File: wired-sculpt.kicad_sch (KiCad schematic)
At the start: 40 parts, among them J1 USB_C_Receptacle, J2 FFC3B07-30-T, J3 AVR-ISP-6 - NOT FITTED, Q1 BSS84AK,215, Q2 2N7002BK,215, SW1 FSMSM, U1 USBLC6-2SC6, U2 LM2776DBVT, U3 AT90USB1286-AUR, Y1 TSX-3225 16.0000MF18X-AC0

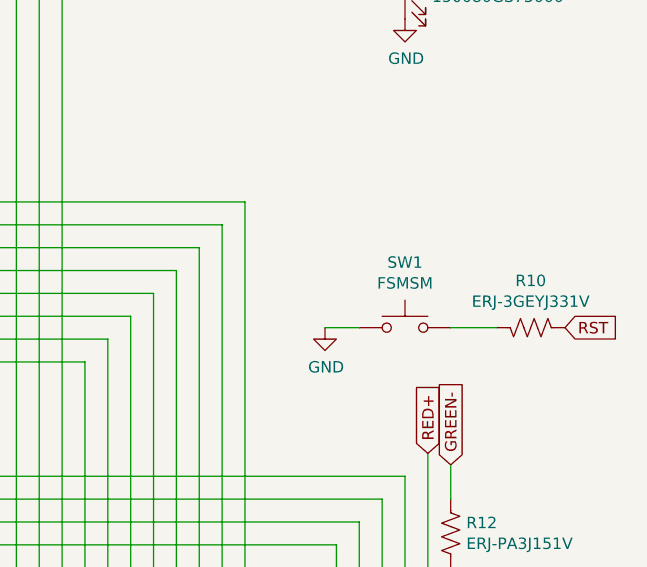
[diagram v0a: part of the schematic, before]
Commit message: Change reset switch to horizontal
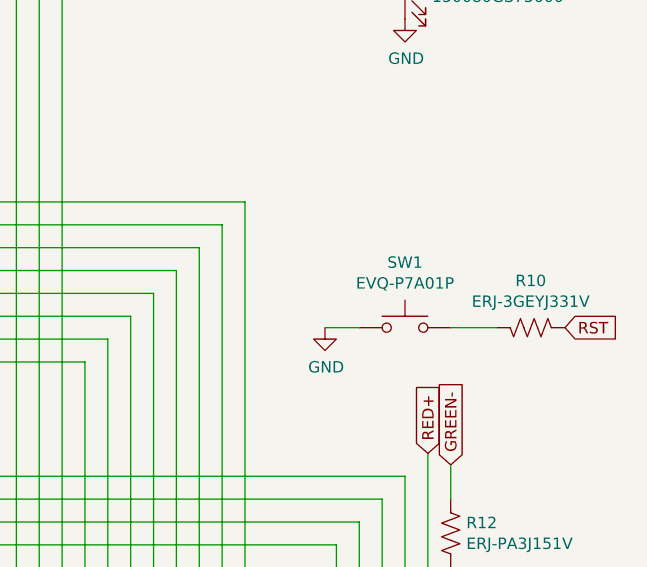
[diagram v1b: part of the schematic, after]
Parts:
- SW1: value FSMSM -> EVQ-P7A01P; footprint Button_Switch_SMD:SW_SPST_FSMSM -> Button_Switch_SMD:SW_SPST_EVQP7A; MPN FSMSM -> EVQ-P7A01P
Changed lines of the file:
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@@
     (in_bom yes) (on_board yes)
     (property "Reference" "SW1" (id 0) (at 234.95 95.631 0))
-    (property "Value" "FSMSM" (id 1) (at 234.95 97.9424 0))
-    (property "Footprint" "Button_Switch_SMD:SW_SPST_FSMSM" (id 2) (at 234.95 97.79 0)
+    (property "Value" "EVQ-P7A01P" (id 1) (at 234.95 97.9424 0))
+    (property "Footprint" "Button_Switch_SMD:SW_SPST_EVQP7A" (id 2) (at 234.95 97.79 0)
       (effects (font (size 1.27 1.27)) hide)
     )
@@
       (effects (font (size 1.27 1.27)) hide)
     )
-    (property "MPN" "FSMSM" (id 4) (at 234.95 102.87 0)
+    (property "MPN" "EVQ-P7A01P" (id 4) (at 234.95 102.87 0)
       (effects (font (size 1.27 1.27)) hide)
     )
@@
     )
     (path "/00000000-0000-0000-0000-00005fce3ca5"
-      (reference "SW1") (unit 1) (value "FSMSM") (footprint "Button_Switch_SMD:SW_SPST_FSMSM")
+      (reference "SW1") (unit 1) (value "EVQ-P7A01P") (footprint "Button_Switch_SMD:SW_SPST_EVQP7A")
     )
     (path "/00000000-0000-0000-0000-00005fcb764b"

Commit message: Increase H3 to 3mm
Slightly more tolerance is needed. Board fit in one of my keyboards, but
not the other
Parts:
- H3: footprint MountingHole:MountingHole_2.7mm -> MountingHole:MountingHole_3mm
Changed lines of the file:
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@@
       (effects (font (size 1.27 1.27)) (justify left))
     )
-    (property "Footprint" "MountingHole:MountingHole_2.7mm" (id 2) (at 132.08 193.04 0)
+    (property "Footprint" "MountingHole:MountingHole_3mm" (id 2) (at 132.08 193.04 0)
       (effects (font (size 1.27 1.27)) hide)
     )
@@
     )
     (path "/00000000-0000-0000-0000-00005fc9a3d1"
-      (reference "H3") (unit 1) (value "AlignmentHole") (footprint "MountingHole:MountingHole_2.7mm")
+      (reference "H3") (unit 1) (value "AlignmentHole") (footprint "MountingHole:MountingHole_3mm")
     )
     (path "/00000000-0000-0000-0000-00005fc1fde4"

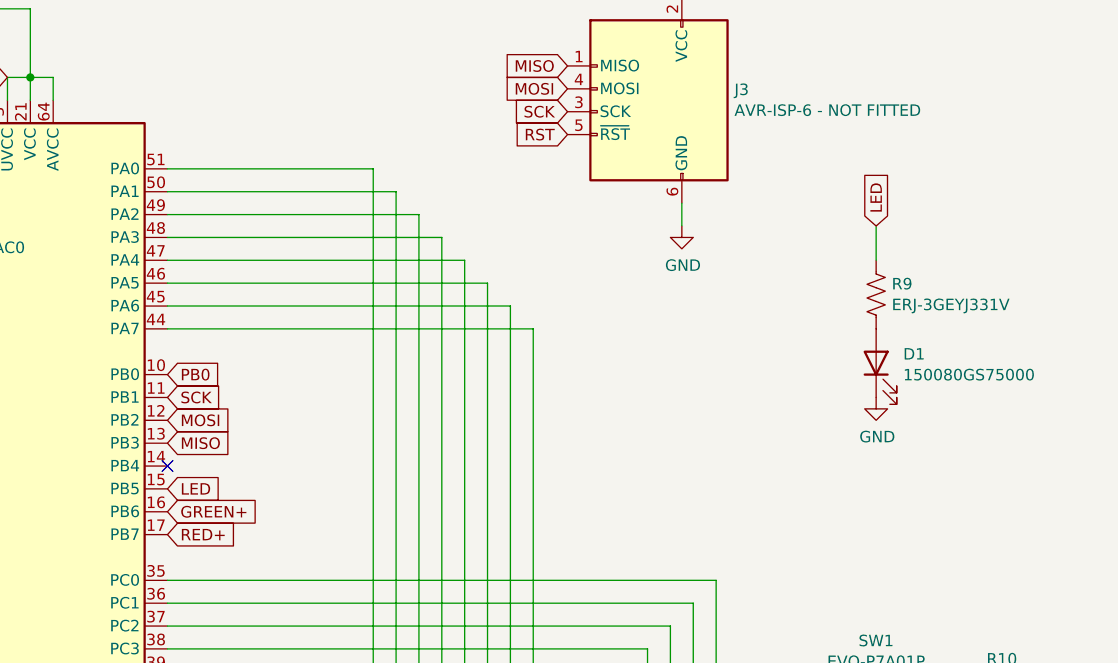
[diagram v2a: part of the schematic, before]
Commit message: Remove on-board status LED
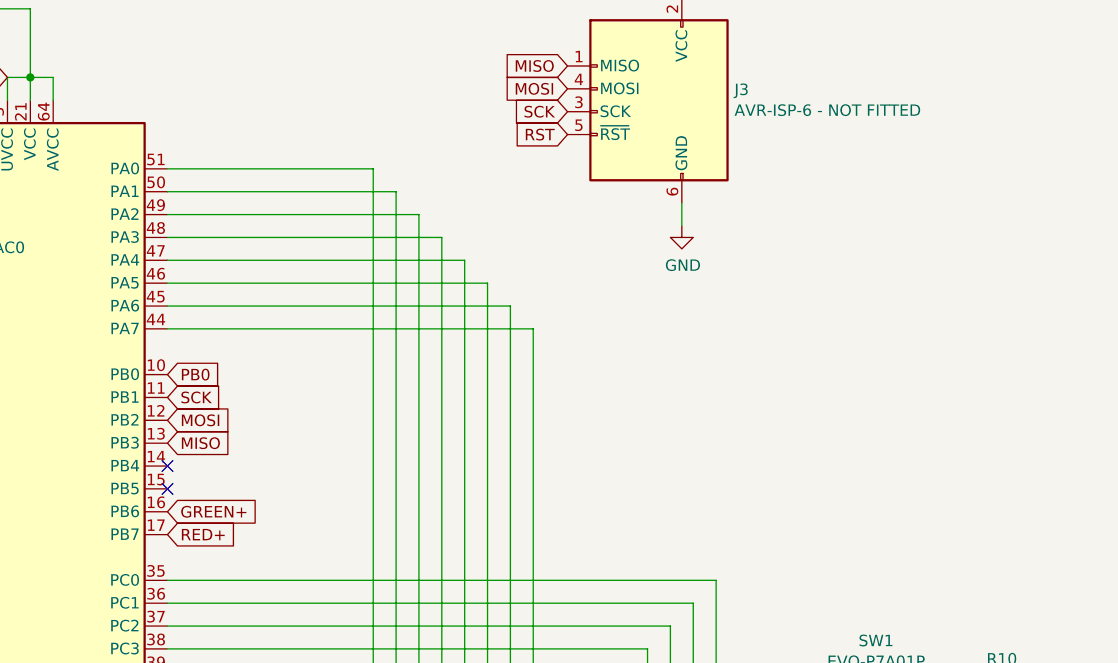
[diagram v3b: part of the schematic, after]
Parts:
- removed D1: 150080GS75000, LED_SMD:LED_0603_1608Metric_Castellated, symbol Device:LED
- removed R9: ERJ-3GEYJ331V, Resistor_SMD:R_0603_1608Metric, symbol Device:R_US
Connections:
- net LED: no longer names the net of U3.15 (PB5)
- no-connect marks 24 -> 25
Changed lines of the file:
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@@
   (no_connect (at 156.21 111.76))
   (no_connect (at 125.73 119.38))
+  (no_connect (at 156.21 78.74))
   (no_connect (at 125.73 111.76))
   (no_connect (at 125.73 116.84))
@@
     (stroke (width 0) (type default) (color 0 0 0 0))
   )
-  (wire (pts (xy 234.95 53.34) (xy 234.95 49.53))
-    (stroke (width 0) (type default) (color 0 0 0 0))
-  )
   (wire (pts (xy 118.11 76.2) (xy 125.73 76.2))
     (stroke (width 0) (type default) (color 0 0 0 0))
@@
     )
   )
-  (global_label "LED" (shape input) (at 234.95 49.53 90) (fields_autoplaced)
-    (effects (font (size 1.27 1.27)) (justify left))
-    (property "Intersheet References" "${INTERSHEET_REFS}" (id 0) (at 0 0 0)
-      (effects (font (size 1.27 1.27)) hide)
-    )
-  )
   (global_label "RED+" (shape input) (at 156.21 83.82 0) (fields_autoplaced)
     (effects (font (size 1.27 1.27)) (justify left))
@@
   )
   (global_label "PE1" (shape input) (at 219.71 151.13 90) (fields_autoplaced)
-    (effects (font (size 1.27 1.27)) (justify left))
-    (property "Intersheet References" "${INTERSHEET_REFS}" (id 0) (at 0 0 0)
-      (effects (font (size 1.27 1.27)) hide)
-    )
-  )
-  (global_label "LED" (shape input) (at 156.21 78.74 0) (fields_autoplaced)
     (effects (font (size 1.27 1.27)) (justify left))
     (property "Intersheet References" "${INTERSHEET_REFS}" (id 0) (at 0 0 0)
@@
     (pin "1")
   )
-  (symbol (lib_id "Device:R_US") (at 234.95 57.15 0) (unit 1)
-    (in_bom yes) (on_board yes)
-    (property "Reference" "R9" (id 0) (at 236.6772 55.9816 0)
-      (effects (font (size 1.27 1.27)) (justify left))
-    )
-    (property "Value" "ERJ-3GEYJ331V" (id 1) (at 236.6772 58.293 0)
-      (effects (font (size 1.27 1.27)) (justify left))
-    )
-    (property "Footprint" "Resistor_SMD:R_0603_1608Metric" (id 2) (at 235.966 57.404 90)
-      (effects (font (size 1.27 1.27)) hide)
-    )
-    (property "Datasheet" "~" (id 3) (at 234.95 57.15 0)
-      (effects (font (size 1.27 1.27)) hide)
-    )
-    (property "MPN" "ERJ-3GEYJ331V" (id 4) (at 234.95 57.15 0)
-      (effects (font (size 1.27 1.27)) hide)
-    )
-    (property "Notes" "330Ohm" (id 5) (at 234.95 57.15 0)
-      (effects (font (size 1.27 1.27)) hide)
-    )
-    (pin "1")
-    (pin "2")
-  )
-  (symbol (lib_id "Device:LED") (at 234.95 64.77 90) (unit 1)
-    (in_bom yes) (on_board yes)
-    (property "Reference" "D1" (id 0) (at 237.9472 63.7794 90)
-      (effects (font (size 1.27 1.27)) (justify right))
-    )
-    (property "Value" "150080GS75000" (id 1) (at 237.9472 66.0908 90)
-      (effects (font (size 1.27 1.27)) (justify right))
-    )
-    (property "Footprint" "LED_SMD:LED_0603_1608Metric_Castellated" (id 2) (at 234.95 64.77 0)
-      (effects (font (size 1.27 1.27)) hide)
-    )
-    (property "Datasheet" "~" (id 3) (at 234.95 64.77 0)
-      (effects (font (size 1.27 1.27)) hide)
-    )
-    (property "MPN" "150080GS75000" (id 4) (at 234.95 64.77 0)
-      (effects (font (size 1.27 1.27)) hide)
-    )
-    (property "Notes" "green led" (id 5) (at 234.95 64.77 0)
-      (effects (font (size 1.27 1.27)) hide)
-    )
-    (pin "1")
-    (pin "2")
-  )
-  (symbol (lib_id "power:GND") (at 234.95 68.58 0) (unit 1)
-    (in_bom yes) (on_board yes)
-    (property "Reference" "#PWR020" (id 0) (at 234.95 74.93 0)
-      (effects (font (size 1.27 1.27)) hide)
-    )
-    (property "Value" "GND" (id 1) (at 235.077 72.9742 0))
-    (property "Footprint" "" (id 2) (at 234.95 68.58 0)
-      (effects (font (size 1.27 1.27)) hide)
-    )
-    (property "Datasheet" "" (id 3) (at 234.95 68.58 0)
-      (effects (font (size 1.27 1.27)) hide)
-    )
-    (pin "1")
-  )
   (symbol (lib_id "Device:C") (at 121.92 29.21 180) (unit 1)
     (in_bom yes) (on_board yes)
@@
       (reference "#PWR019") (unit 1) (value "GND") (footprint "")
     )
-    (path "/00000000-0000-0000-0000-00005fd2e726"
-      (reference "#PWR020") (unit 1) (value "GND") (footprint "")
-    )
     (path "/00000000-0000-0000-0000-0000607d105e"
       (reference "#PWR021") (unit 1) (value "-5V") (footprint "")
@@
       (reference "C12") (unit 1) (value "CL10B104KB8NNNC") (footprint "Capacitor_SMD:C_0603_1608Metric")
     )
-    (path "/00000000-0000-0000-0000-00005fd2cf2a"
-      (reference "D1") (unit 1) (value "150080GS75000") (footprint "LED_SMD:LED_0603_1608Metric_Castellated")
-    )
     (path "/00000000-0000-0000-0000-00005fc615f3"
       (reference "H1") (unit 1) (value "MountingHoleNorth") (footprint "MountingHole:MountingHole_2.2mm_M2")
@@
       (reference "R8") (unit 1) (value "ERJ-PA3J472V") (footprint "Resistor_SMD:R_0603_1608Metric")
     )
-    (path "/00000000-0000-0000-0000-00005fd29e76"
-      (reference "R9") (unit 1) (value "ERJ-3GEYJ331V") (footprint "Resistor_SMD:R_0603_1608Metric")
-    )
     (path "/00000000-0000-0000-0000-00005fd76786"
